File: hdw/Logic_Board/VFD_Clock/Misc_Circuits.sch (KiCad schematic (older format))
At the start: 18 parts

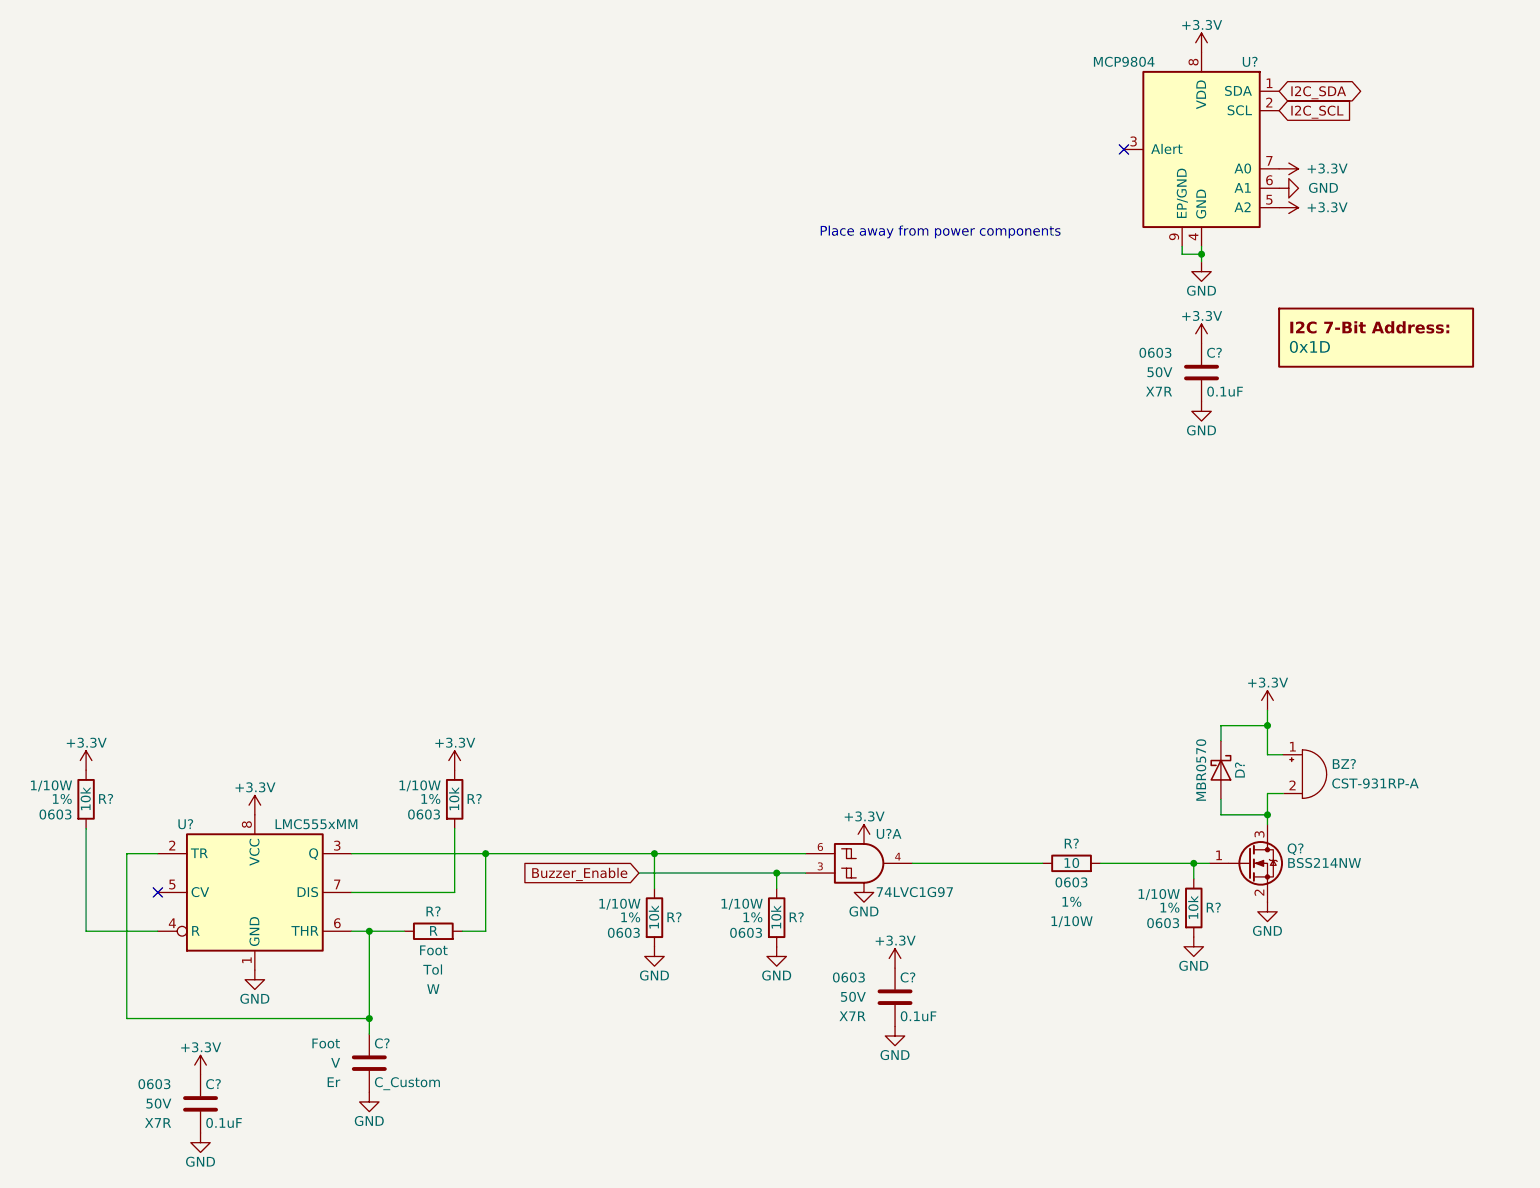
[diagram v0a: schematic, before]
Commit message: Few fixes, added BLE
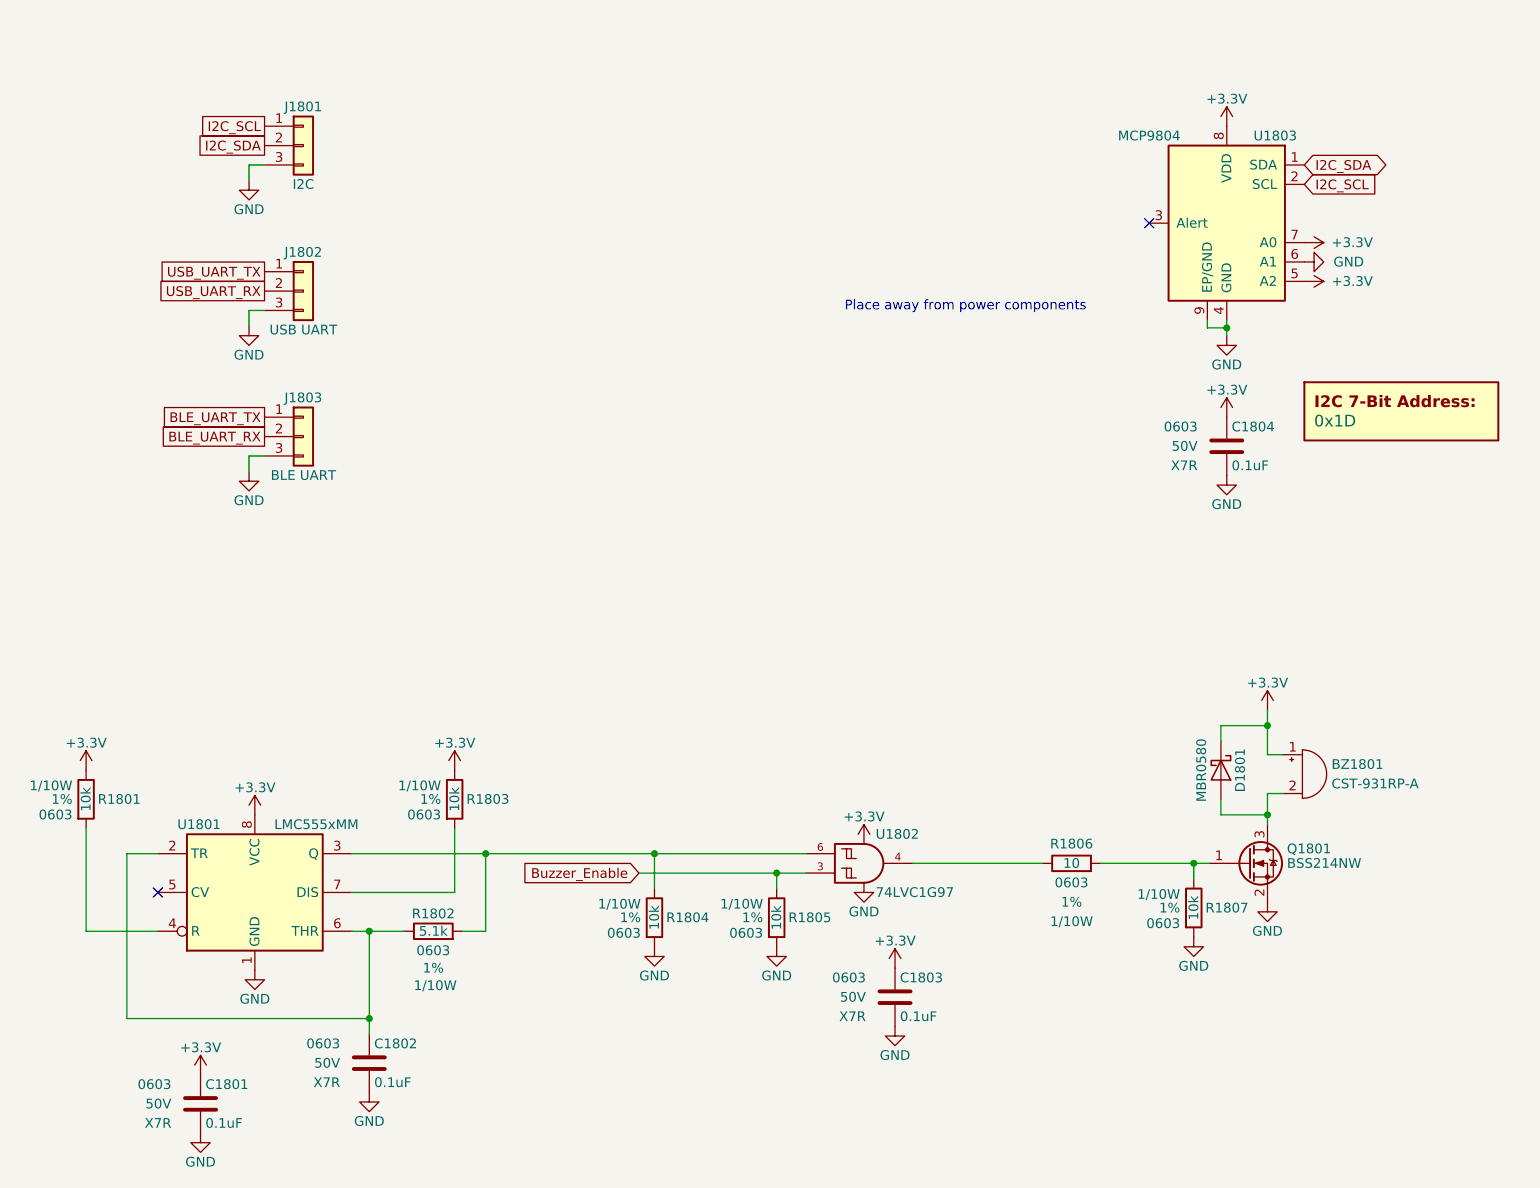
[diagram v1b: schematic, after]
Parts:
- removed C?: C_Custom, symbol Custom_Library:C_Custom
- removed D?: MBR0570, Diode_SMD:D_SOD-123, symbol Diode:MBR0570
- removed R?: R, symbol Custom_Library:R_Custom
- removed U?: 74LVC1G97, Package_TO_SOT_SMD:SOT-363_SC-70-6, symbol Custom_Library:74LVC1G97_Power
- added C1802: 0.1uF, Capacitors_SMD:C_0603, symbol Custom_Library:C_Custom
- added D1801: MBR0580, Diode_SMD:D_SOD-123, symbol Diode:MBR0580
- added J1801: I2C, Pin_Headers:Pin_Header_Straight_1x03_Pitch2.54mm, symbol Connector_Generic:Conn_01x03
- added J1802: USB UART, Pin_Headers:Pin_Header_Straight_1x03_Pitch2.54mm, symbol Connector_Generic:Conn_01x03
- added J1803: BLE UART, Pin_Headers:Pin_Header_Straight_1x03_Pitch2.54mm, symbol Connector_Generic:Conn_01x03
- added R1802: 5.1k, Resistors_SMD:R_0603, symbol Custom_Library:R_Custom
- added U1802: 74LVC1G97, Package_TO_SOT_SMD:SOT-363_SC-70-6, symbol Custom_Library:74LVC1G97_Power_AND
- BZ1801: renamed from BZ?; Digi-Key PN (none) -> 439-1070-ND
- U1801: renamed from U?; footprint (none) -> Package_SO:VSSOP-8_3.0x3.0mm_P0.65mm; Digi-Key PN (none) -> LMC555CMM/NOPBCT-ND
- U1803: renamed from U?; Digi-Key PN (none) -> MCP9804T-E/MCCT-ND
- gave numbers to parts that had none: 11
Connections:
- net +3V3: now also D1801.1 (K), U1802.5 (VCC)
- net Buzzer_Enable: now also U1802.3
- net GND: now also C1802.2, J1801.3 (Pin_3), J1802.3 (Pin_3), J1803.3 (Pin_3), U1802.1 (GND), U1802.2 (GND)
- net I2C_SCL: now also J1801.1 (Pin_1)
- net I2C_SDA: now also J1801.2 (Pin_2)
- net at BZ1801.2 (+), Q1801.3 (D): now also D1801.2 (A)
- net at U1801.2 (TR), U1801.6 (THR): now also C1802.1, R1802.2
- net at R1804.2, U1801.3 (Q): now also R1802.1, U1802.6
- net at R1806.2: now also U1802.4
- new net BLE_UART_RX: J1803.2 (Pin_2)
- new net BLE_UART_TX: J1803.1 (Pin_1)
- new net USB_UART_RX: J1802.2 (Pin_2)
- new net USB_UART_TX: J1802.1 (Pin_1)
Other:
- moved on the sheet: C1804, U1803

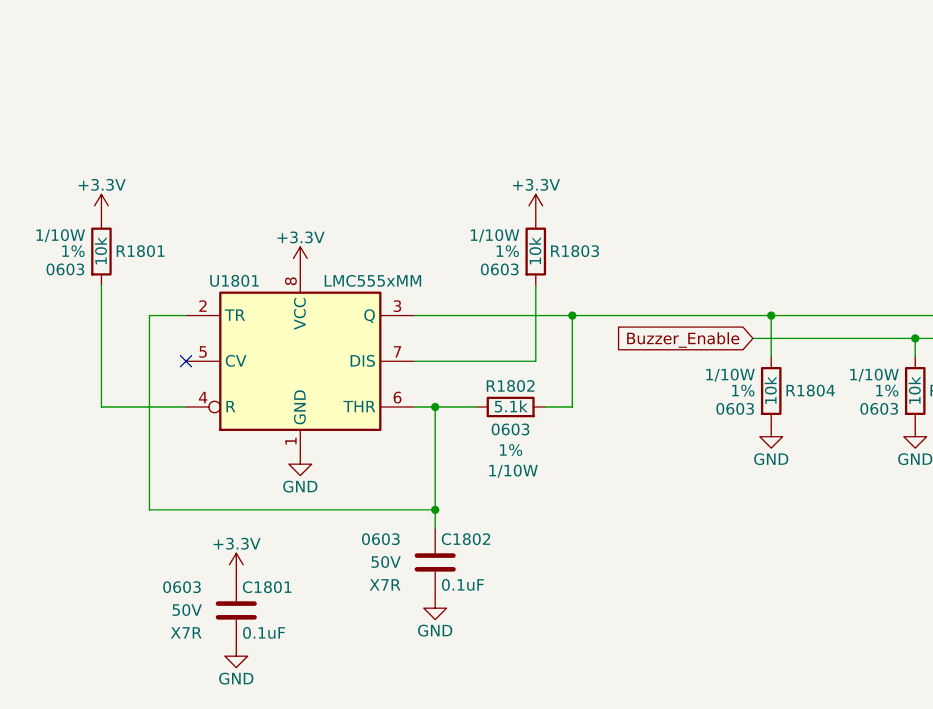
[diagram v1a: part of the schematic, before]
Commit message: Changed buzzer clock, netlist changes
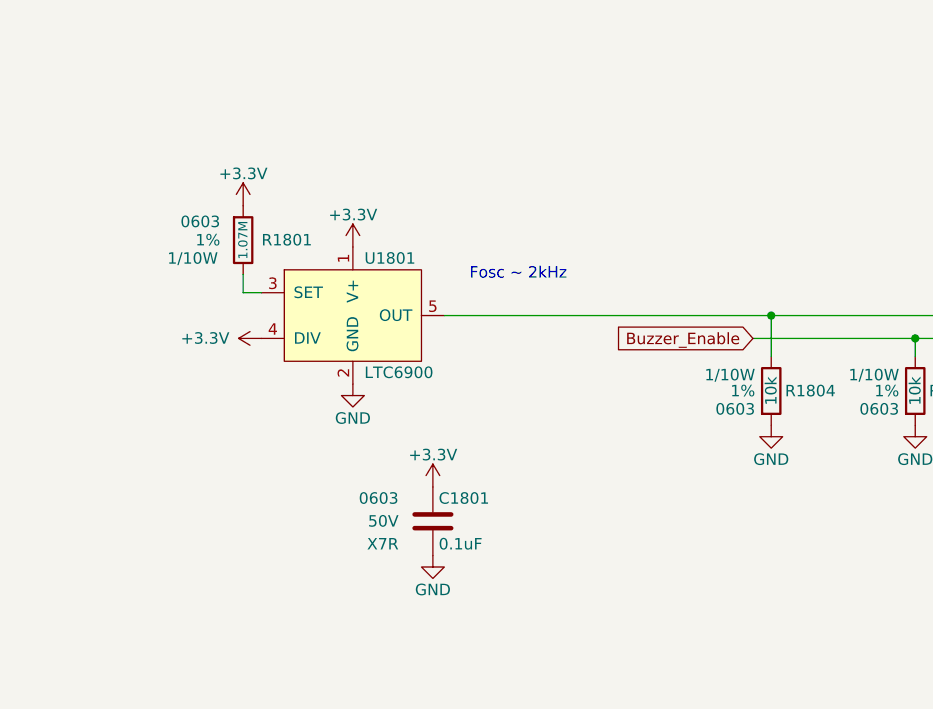
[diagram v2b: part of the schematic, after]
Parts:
- removed C1802: 0.1uF, Capacitors_SMD:C_0603, symbol Custom_Library:C_Custom
- removed R1802: 5.1k, Resistors_SMD:R_0603, symbol Custom_Library:R_Custom
- removed R1803: 10k, Resistors_SMD:R_0603, symbol Custom_Library:R_Custom
- removed U1801: LMC555xMM, Package_SO:VSSOP-8_3.0x3.0mm_P0.65mm, symbol Timer:LMC555xMM
- added U1801: LTC6900, Package_TO_SOT_SMD:SOT-23-5, symbol Custom_Library:LTC6900
- R1801: value 10k -> 1.07M; Digi-Key PN P10.0KHCT-ND -> 541-1.07MHCT-ND
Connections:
- net +3V3: now also R1801.1, U1801.1 (V+), U1801.4 (DIV); no longer R1801.2
- net GND: now also U1801.2 (GND)
- net at R1804.2, U1802.6: now also U1801.5 (OUT)
- new net: R1801.2, U1801.3 (SET)
- no-connect marks 2 -> 1
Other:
- note added: "Fosc ~~ 2kHz"
